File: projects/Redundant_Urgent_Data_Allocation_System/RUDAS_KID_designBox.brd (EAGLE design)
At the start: 99 x 64.2 mm, 46 parts, among them IC2 STM32F103VGT6, IC3 5M240ZT100

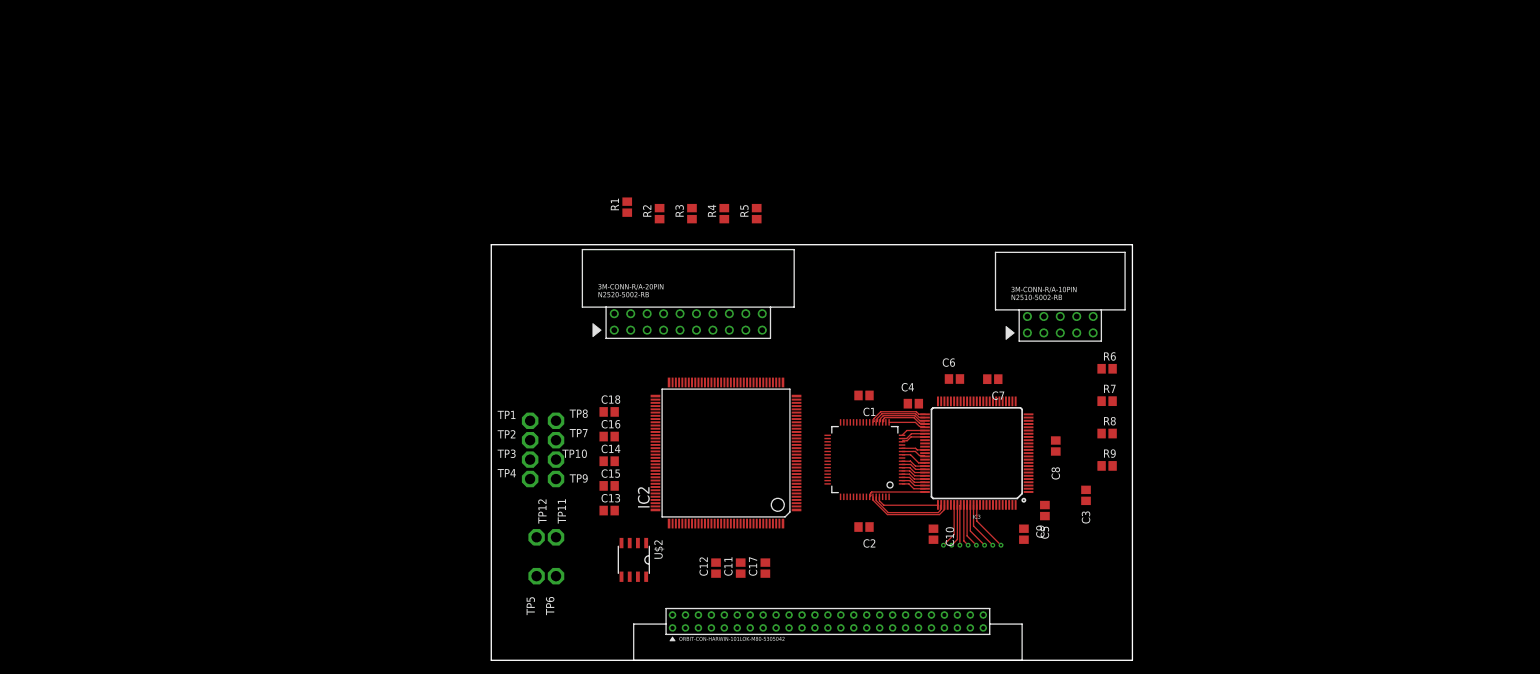
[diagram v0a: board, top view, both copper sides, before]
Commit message: add new part list
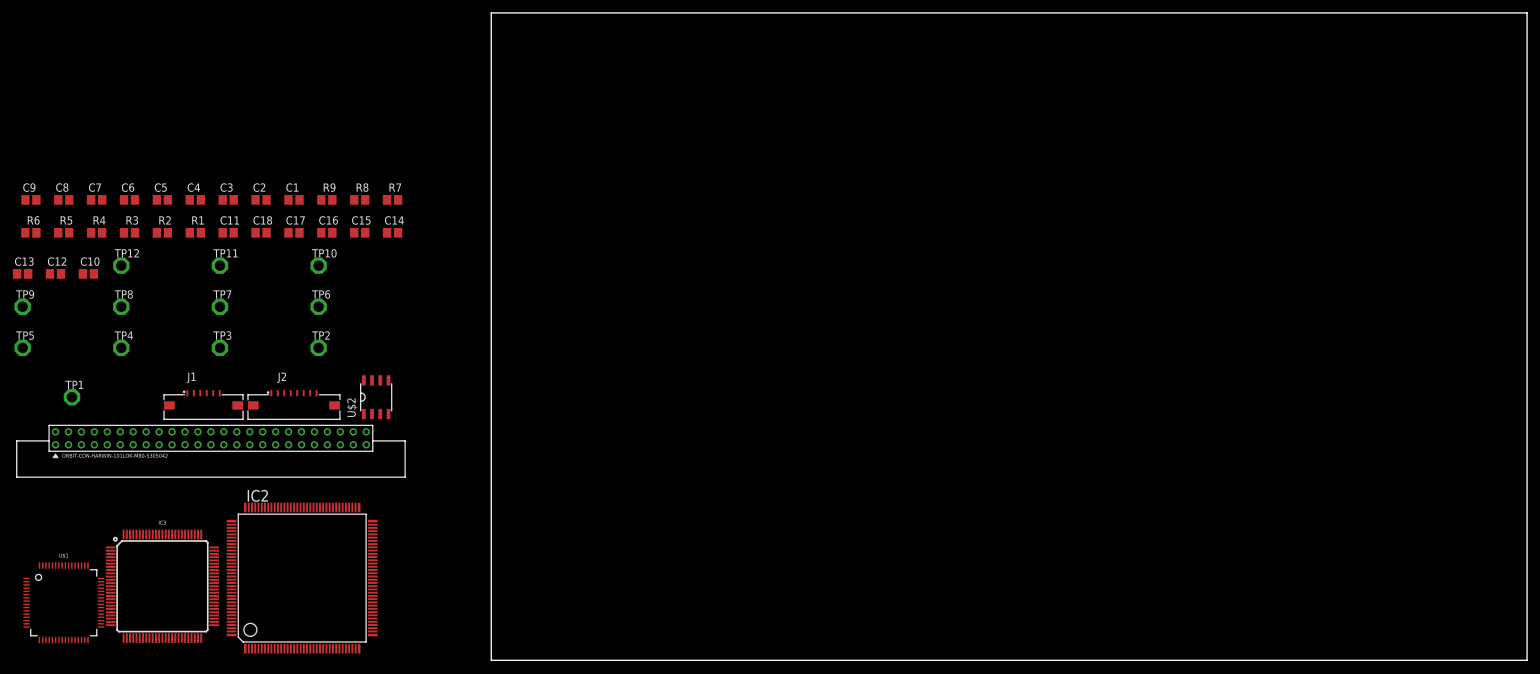
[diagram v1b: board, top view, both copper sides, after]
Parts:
- removed U$3: CONN-10PINR/A-10PIN, ORBIT-CONN HEADER-3M-2500 Series:R/A-10PIN
- removed U$4: CONN-20PINR/A-20PIN, ORBIT-CONN HEADER-3M-2500 Series:R/A-20PIN
- added J1: (no value), Wurth_Elektronik_Electromechanic_FPC_Connectors_&_Flat_Flexible_Cable_rev18c:686106183522
- added J2: (no value), Wurth_Elektronik_Electromechanic_FPC_Connectors_&_Flat_Flexible_Cable_rev18c:686108183422
- moved R6 167.6 mm to (-71.1, 66.0)
- moved C9 161.9 mm to (-71.1, 71.1), turned to 0 degrees
- moved C8 157.9 mm to (-66.0, 71.1), turned to 0 degrees
- moved C5 144.5 mm to (-50.8, 71.1), turned to 0 degrees
- moved C7 141.2 mm to (-61.0, 71.1), turned to 0 degrees
- moved C3 140.1 mm to (-40.6, 71.1), turned to 0 degrees
- moved C10 136.6 mm to (-62.2, 59.7), turned to 0 degrees
- moved C6 130.4 mm to (-55.9, 71.1)
- moved IC3 127.5 mm to (-50.8, 11.4), turned to 0 degrees
- moved R9 127.3 mm to (-25.4, 71.1)
- moved U$1 125.7 mm to (-66.0, 8.89), turned to 0 degrees
- moved R8 121.0 mm to (-20.3, 71.1)
- moved C4 115.3 mm to (-45.7, 71.1)
- moved R7 114.7 mm to (-15.2, 71.1)
- moved C12 111.7 mm to (-67.3, 59.7), turned to 0 degrees
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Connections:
- net N$10 renamed 12V_GND
- net N$11 renamed +5V
- net N$12 renamed 3V_GND
- net N$5 renamed CAN_H_S
- net N$6 renamed CAN_L_S
- net N$7 renamed +12V
- net N$8 renamed 5V_GND
- net N$9 renamed +3V
- net CPLD_GND: now also J1.1; no longer U$3.PIN10, U$3.PIN6
- net CPLD_IO_VCC: now also J1.6; no longer U$3.PIN7, U$3.PIN8
- net C_TCK: now also J1.5; no longer U$3.PIN1
- net C_TDI: now also J1.2; no longer U$3.PIN5
- net C_TDO: now also J1.4; no longer U$3.PIN2
- net C_TMS: now also J1.3; no longer U$3.PIN3
- net LAN_CLK_N2: now also IC3.96
- net LAN_CLK_N3: now also IC3.29
- net LAN_CLK_N4: now also IC3.19
- net LAN_CLK_N5: now also IC3.5
- net LAN_CLK_P2: now also IC3.97
- net LAN_CLK_P3: now also IC3.28
- net LAN_CLK_P4: now also IC3.18
- net LAN_CLK_P5: now also IC3.4
- net LAN_N2: now also IC3.98
- net LAN_N3: now also IC3.27
- net LAN_N4: now also IC3.17
- net LAN_N5: now also IC3.3
- net LAN_P2: now also IC3.99
- net LAN_P3: now also IC3.26
- net LAN_P4: now also IC3.16
- net LAN_P5: now also IC3.2
- net S_GND: now also J2.1; no longer U$4.PIN12, U$4.PIN13, U$4.PIN14, U$4.PIN15, U$4.PIN16, U$4.PIN17, U$4.PIN18, U$4.PIN19, U$4.PIN20
- net S_RST: now also J2.2; no longer U$4.PIN9
- net S_TCK: now also J2.4; no longer U$4.PIN5
- net S_TDI: now also J2.6; no longer U$4.PIN3
- net S_TDO: now also J2.3; no longer U$4.PIN7
- net S_TMS: now also J2.5; no longer U$4.PIN4
- net S_TRST: now also J2.7; no longer U$4.PIN2
- net S_VCC: now also J2.8; no longer U$4.PIN1, U$4.PIN11
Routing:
- net LAN_CLK_N0: track 43.0 -> 0.00 mm, vias 1 -> 0
- net LAN_CLK_P0: track 41.7 -> 0.00 mm, vias 1 -> 0
- net LAN_N0: track 41.1 -> 0.00 mm, vias 1 -> 0
- net LAN_P0: track 39.5 -> 0.00 mm, vias 1 -> 0
- net LAN_CLK_N1: track 34.1 -> 0.00 mm, vias 1 -> 0
- net LAN_CLK_P1: track 33.4 -> 0.00 mm, vias 1 -> 0
- net LAN_N1: track 31.9 -> 0.00 mm, vias 1 -> 0
- net LAN_P1: track 31.2 -> 0.00 mm, vias 1 -> 0
- net R/!W!: track 13.5 -> 0.00 mm
- net !BUSY!: track 12.3 -> 0.00 mm
- net !INT!: track 9.98 -> 0.00 mm
- net D7: track 9.14 -> 0.00 mm
- net !CE!: track 9.11 -> 0.00 mm
- net D6: track 8.60 -> 0.00 mm
- net D5: track 8.05 -> 0.00 mm
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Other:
- board size 99 x 64.2 mm -> 160 x 100 mm
